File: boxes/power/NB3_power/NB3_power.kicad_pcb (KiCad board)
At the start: 2 copper layers, 80 x 97 mm, 87 parts, among them J1 Barrel_Jack_PJ-036AH-SMT-TR, J2 Conn_01x02_Male, J3 Conn_01x02_Male, J4 Conn_01x02_Male, J5 Conn_01x04_Male, J6 Conn_01x02_Male, J7 Conn_01x02_Male, Q1 PMOS, Q2 NMOS, SW1 SW_SPDT, U1 NiMH_Charger_LTC4010, U2 Voltage_Regulator_AP64501

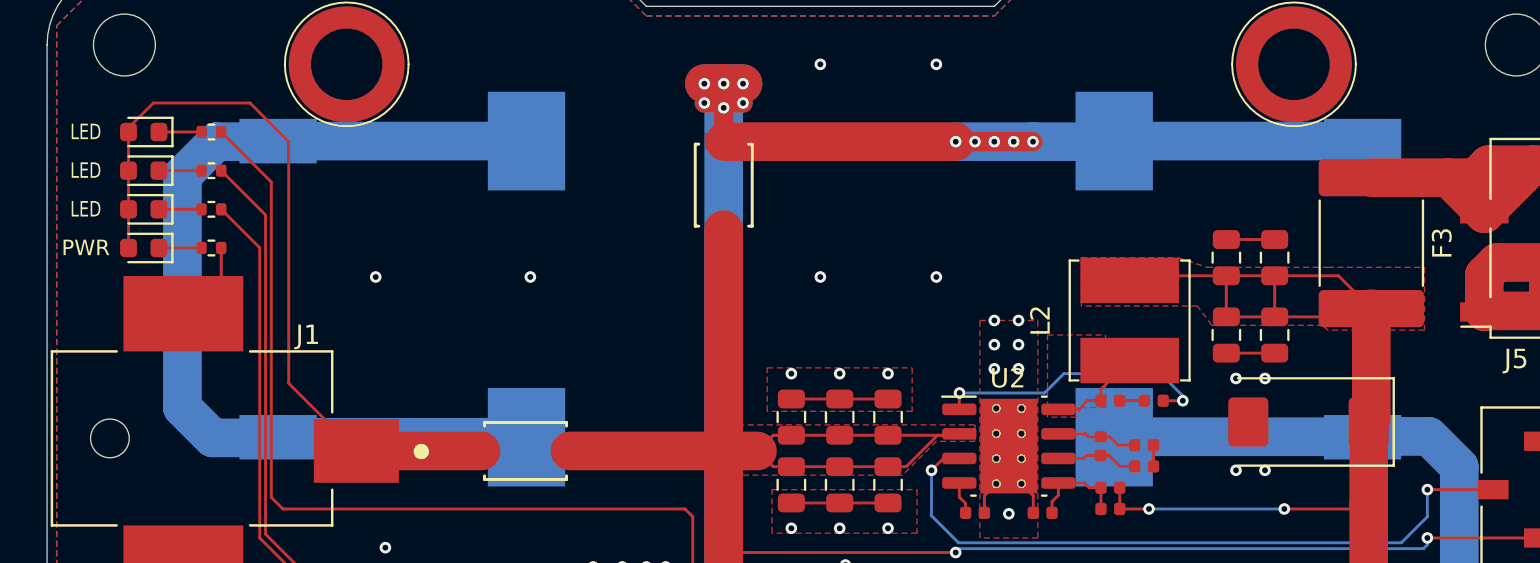
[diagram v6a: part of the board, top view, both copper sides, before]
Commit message: NB3_power PCB fab submisson
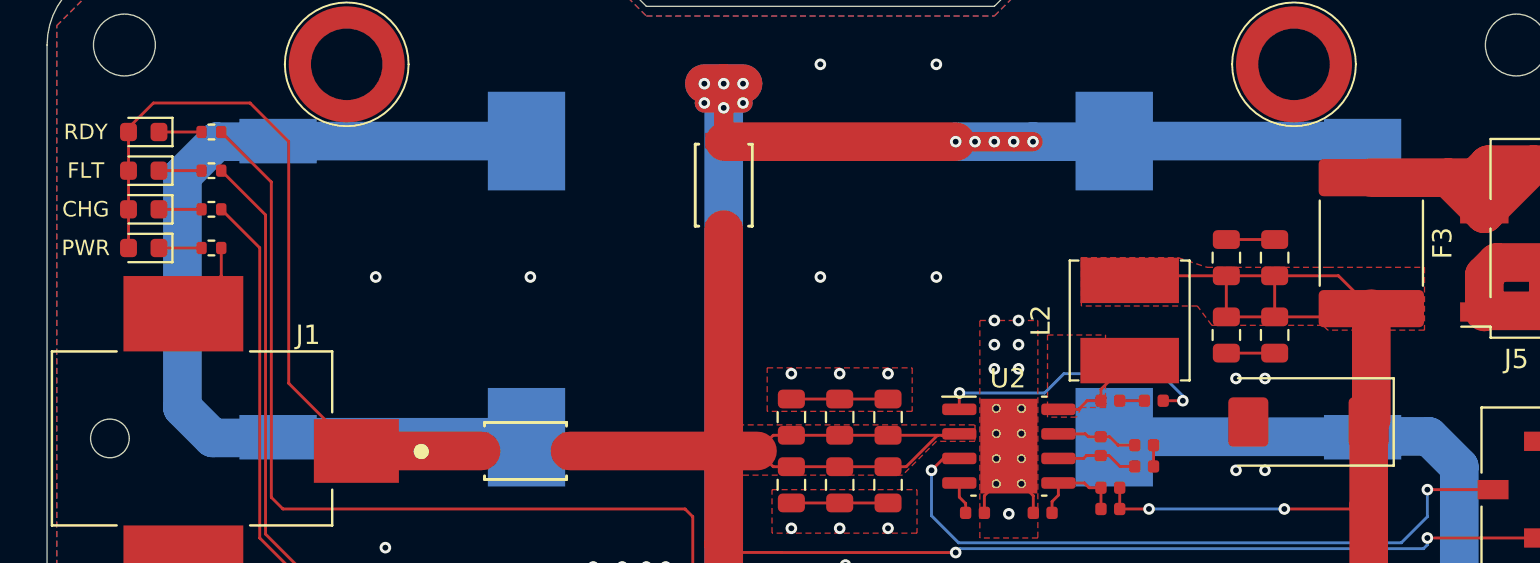
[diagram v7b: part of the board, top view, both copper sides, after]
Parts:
- C1, C2: value 20uF -> 22uF
- R1, R2, R3, R4: value 560 -> 5.6k
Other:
- board text added: "CHG"
- board text added: "FLT"
- board text added: "RDY"
- board text removed: "LED"
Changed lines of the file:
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@@
       (layerselection 0x00010fc_ffffffff)
       (disableapertmacros false)
-      (usegerberextensions false)
+      (usegerberextensions true)
       (usegerberattributes false)
       (usegerberadvancedattributes false)
@@
       (viasonmask false)
       (mode 1)
-      (useauxorigin false)
+      (useauxorigin true)
       (hpglpennumber 1)
       (hpglpenspeed 20)
@@
       (plotreference true)
       (plotvalue true)
-      (plotinvisibletext false)
+      (plotinvisibletext true)
       (sketchpadsonfab false)
       (subtractmaskfromsilk false)
       (outputformat 1)
       (mirror false)
-      (drillshape 1)
+      (drillshape 0)
       (scaleselection 1)
-      (outputdirectory "")
+      (outputdirectory "fab/")
     )
   )
@@
       (effects (font (size 1 1) (thickness 0.15)))
     )
-    (fp_text value "20uF" (at 0 1.65 90) (layer "F.Fab")
+    (fp_text value "22uF" (at 0 1.65 90) (layer "F.Fab")
       (effects (font (size 1 1) (thickness 0.15)))
     )
@@
     (fp_line (start -2.65 -2.15) (end -3.65 -1.15) (layer "F.Fab") (width 0.1))
     (fp_line (start -3.65 -1.15) (end -3.65 2.15) (layer "F.Fab") (width 0.1))
-    (pad "1" smd roundrect (at -3.1125 0 180) (size 2.075 2.55) (layers "F.Cu" "F.Paste" "F.Mask") (roundrect_rratio 0.120482)
+    (pad "1" smd roundrect (at -3.1125 0 180) (size 2.075 2.55) (layers "F.Cu" "F.Paste" "F.Mask") (roundrect_rratio 0.1204819277108434)
       (net 20 "+5V"))
-    (pad "2" smd roundrect (at 3.1125 0 180) (size 2.075 2.55) (layers "F.Cu" "F.Paste" "F.Mask") (roundrect_rratio 0.120482)
+    (pad "2" smd roundrect (at 3.1125 0 180) (size 2.075 2.55) (layers "F.Cu" "F.Paste" "F.Mask") (roundrect_rratio 0.1204819277108434)
       (net 2 "GND"))
     (model "${KISYS3DMOD}/Capacitor_Tantalum_SMD.3dshapes/CP_EIA-7343-31_Kemet-D.wrl"
@@
       (effects (font (size 1 1) (thickness 0.15)))
     )
-    (fp_text value "Conn_01x02_Male" (at 0 3.6 180) (layer "F.Fab")
+    (fp_text value "Conn_01x02_Male" (at 0 3.6 180) (layer "F.Fab") hide
       (effects (font (size 1 1) (thickness 0.15)))
     )
@@
       (effects (font (size 1 1) (thickness 0.15)))
     )
-    (fp_text value "560" (at 0 1.17 180) (layer "F.Fab")
+    (fp_text value "5.6k" (at 0 1.17 180) (layer "F.Fab")
       (effects (font (size 1 1) (thickness 0.15)))
     )
@@
       (effects (font (size 1 1) (thickness 0.15)))
     )
-    (fp_text value "MountingHole_3.2mm_M3" (at 0 4.2) (layer "F.Fab")
+    (fp_text value "MountingHole_3.2mm_M3" (at 0 4.2) (layer "F.Fab") hide
       (effects (font (size 1 1) (thickness 0.15)))
     )
@@
       (effects (font (size 1 1) (thickness 0.15)))
     )
-    (fp_text value "Conn_01x02_Male" (at 0 3.6 -90) (layer "F.Fab")
+    (fp_text value "Conn_01x02_Male" (at 0 3.6 -90) (layer "F.Fab") hide
       (effects (font (size 1 1) (thickness 0.15)))
     )
@@
       (effects (font (size 1 1) (thickness 0.15)))
     )
-    (fp_text value "560" (at 0 1.17) (layer "F.Fab")
+    (fp_text value "5.6k" (at 0 1.17) (layer "F.Fab")
       (effects (font (size 1 1) (thickness 0.15)))
     )
@@
       (effects (font (size 1 1) (thickness 0.15)))
     )
-    (fp_text value "560" (at 0 1.17) (layer "F.Fab")
+    (fp_text value "5.6k" (at 0 1.17) (layer "F.Fab")
       (effects (font (size 1 1) (thickness 0.15)))
     )
@@
     (fp_line (start 3.6775 2.56) (end -3.6775 2.56) (layer "F.Fab") (width 0.1))
     (fp_line (start 3.6775 -2.56) (end 3.6775 2.56) (layer "F.Fab") (width 0.1))
-    (pad "1" smd roundrect (at -3.3875 0 270) (size 1.925 5.45) (layers "F.Cu" "F.Paste" "F.Mask") (roundrect_rratio 0.12987)
+    (pad "1" smd roundrect (at -3.3875 0 270) (size 1.925 5.45) (layers "F.Cu" "F.Paste" "F.Mask") (roundrect_rratio 0.1298701298701299)
       (net 10 "Net-(F3-Pad1)"))
-    (pad "2" smd roundrect (at 3.3875 0 270) (size 1.925 5.45) (layers "F.Cu" "F.Paste" "F.Mask") (roundrect_rratio 0.12987)
+    (pad "2" smd roundrect (at 3.3875 0 270) (size 1.925 5.45) (layers "F.Cu" "F.Paste" "F.Mask") (roundrect_rratio 0.1298701298701299)
       (net 20 "+5V"))
     (model "${KIPRJMOD}/libraries/parts/Fuse_3A_MF-LSMF300X-2/Fuse_3A_MF-LSMF300X-2.stp"
@@
       (effects (font (size 1 1) (thickness 0.15)))
     )
-    (fp_text value "MountingHole_3.2mm_M3" (at 0 4.2) (layer "F.Fab")
+    (fp_text value "MountingHole_3.2mm_M3" (at 0 4.2) (layer "F.Fab") hide
       (effects (font (size 1 1) (thickness 0.15)))
     )
@@
       (effects (font (size 1 1) (thickness 0.15)))
     )
-    (fp_text value "Conn_01x02_Male" (at 0 3.6 -90) (layer "F.Fab")
+    (fp_text value "Conn_01x02_Male" (at 0 3.6 -90) (layer "F.Fab") hide
       (effects (font (size 1 1) (thickness 0.15)))
     )
@@
       (effects (font (size 1 1) (thickness 0.15)))
     )
-    (fp_text value "Conn_01x04_Male" (at 0 6.14 180) (layer "F.Fab")
+    (fp_text value "Conn_01x04_Male" (at 0 6.14 180) (layer "F.Fab") hide
       (effects (font (size 1 1) (thickness 0.15)))
     )
@@
       (effects (font (size 1 1) (thickness 0.15)))
     )
-    (fp_text value "Conn_01x02_Male" (at 0 3.6 180) (layer "F.Fab")
+    (fp_text value "Conn_01x02_Male" (at 0 3.6 180) (layer "F.Fab") hide
       (effects (font (size 1 1) (thickness 0.15)))
     )
@@
       (effects (font (size 1 1) (thickness 0.15)))
     )
-    (fp_text value "Conn_01x02_Male" (at 0 3.6 -90) (layer "F.Fab")
+    (fp_text value "Conn_01x02_Male" (at 0 3.6 -90) (layer "F.Fab") hide
       (effects (font (size 1 1) (thickness 0.15)))
     )
@@
       (effects (font (size 1 1) (thickness 0.15)))
     )
-    (fp_text value "560" (at 0 1.17 180) (layer "F.Fab")
+    (fp_text value "5.6k" (at 0 1.17 180) (layer "F.Fab")
       (effects (font (size 1 1) (thickness 0.15)))
     )
@@
       (effects (font (size 1 1) (thickness 0.15)))
     )
-    (fp_text value "MountingHole_3.2mm_M3" (at 0 4.2) (layer "F.Fab")
+    (fp_text value "MountingHole_3.2mm_M3" (at 0 4.2) (layer "F.Fab") hide
       (effects (font (size 1 1) (thickness 0.15)))
     )
@@
       (effects (font (size 1 1) (thickness 0.15)))
     )
-    (fp_text value "MountingHole_3.2mm_M3" (at 0 4.2) (layer "F.Fab")
+    (fp_text value "MountingHole_3.2mm_M3" (at 0 4.2) (layer "F.Fab") hide
       (effects (font (size 1 1) (thickness 0.15)))
     )
@@
       (effects (font (size 1 1) (thickness 0.15)))
     )
-    (fp_text value "20uF" (at 0 1.65) (layer "F.Fab")
+    (fp_text value "22uF" (at 0 1.65) (layer "F.Fab")
       (effects (font (size 1 1) (thickness 0.15)))
     )
@@
   (gr_line (start 157.05 50.83) (end 159.05 48.83) (layer "Edge.Cuts") (width 0.05))
   (gr_arc (start 186.05 143.83) (end 188.05 143.83) (angle 90) (layer "Edge.Cuts") (width 0.05))
-  (gr_text "LED" (at 110.05 57.33) (layer "F.SilkS")
-    (effects (font (size 0.8 0.6) (thickness 0.15)))
+  (gr_text "RDY" (at 110.05 57.33) (layer "F.SilkS")
+    (effects (font (size 0.8 0.8) (thickness 0.15)))
   )
   (gr_text "NB3 POWER" (at 148.05 129.83) (layer "F.SilkS")
     (effects (font (size 2 2) (thickness 0.3)))
   )
-  (gr_text "LED" (at 110.05 61.33) (layer "F.SilkS")
-    (effects (font (size 0.8 0.6) (thickness 0.15)))
+  (gr_text "CHG" (at 110.05 61.33) (layer "F.SilkS")
+    (effects (font (size 0.8 0.8) (thickness 0.15)))
   )
   (gr_text "PWR" (at 110.05 63.33) (layer "F.SilkS")
     (effects (font (size 0.8 0.8) (thickness 0.15)))
   )
-  (gr_text "LED" (at 110.05 59.33) (layer "F.SilkS")
-    (effects (font (size 0.8 0.6) (thickness 0.15)))
+  (gr_text "FLT" (at 110.05 59.33) (layer "F.SilkS")
+    (effects (font (size 0.8 0.8) (thickness 0.15)))
   )
   (target plus (at 148.05 151.83) (size 5) (width 0.05) (layer "Edge.Cuts"))

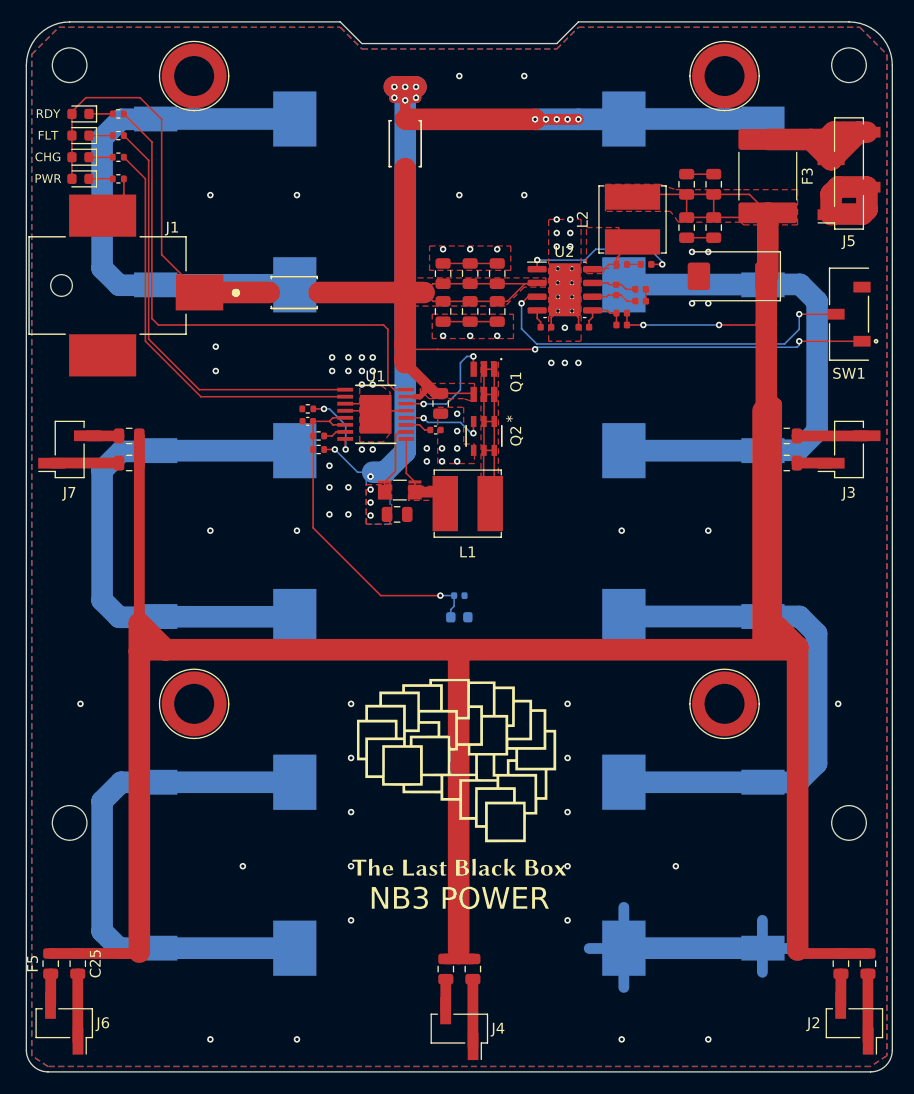
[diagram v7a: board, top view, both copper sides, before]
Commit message: Added new NB3 board drafts (body and power)
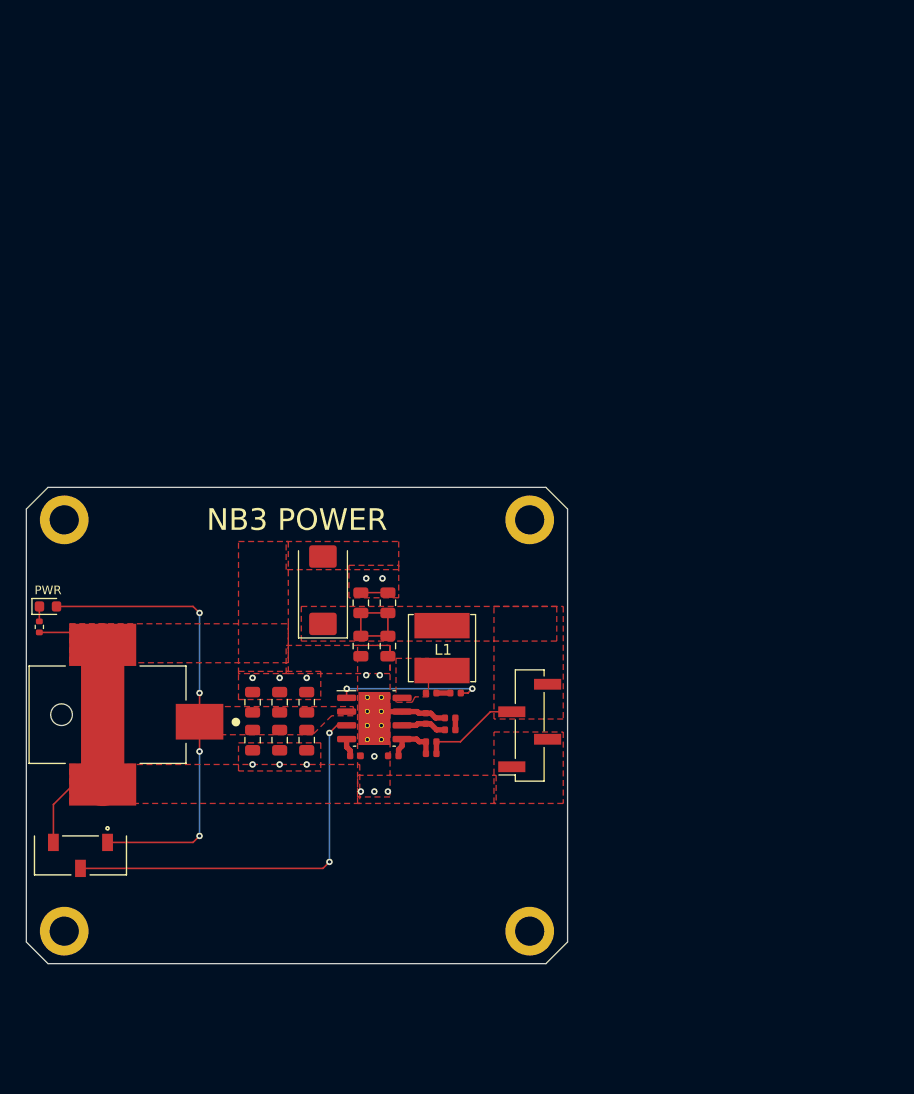
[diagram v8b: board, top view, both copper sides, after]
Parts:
- removed the C1 at (146.3, 84.1)
- removed the C2 at (142.3, 94.3)
- removed C22, C23, C24, C25, C26: 10uF, Capacitor_SMD:C_0805_2012Metric
- removed the C3 at (145.8, 86.5)
- removed the C4 at (134.1, 85.7)
- removed the C5 at (148.1, 101.8)
- removed CR1, CR2: Schottky_PMEG3050EP,115, NB3_power:Schottky_PMEG3050EP,115
- removed the D1 at (113.0, 57.3)
- removed D2, D3: LED, LED_SMD:LED_0603_1608Metric
- removed F1, F2, F4, F5, F6: 1.1h2.2t, Fuse:Fuse_0805_2012Metric
- removed F3: 3h5t, Fuse:Fuse_2920_7451Metric
- removed G***: LOGO, NB3_power:Logo_LBB_25mm
- removed G***: LOGO, NB3_power:Logo_VK_15mm
- removed the J2 at (184.6, 141.3)
- removed J3, J4, J6, J7: Conn_01x02_Male, Connector_PinHeader_2.54mm:PinHeader_1x02_P2.54mm_Vertical_SMD_Pin1Right
- removed the L1 at (148.8, 93.3)
- removed Q1: PMOS, NB3_power:PMOS_SMD_FDC658AP
- removed Q2: NMOS, NB3_power:NMOS_SMD_SI3410DV-T1-GE3
- removed the R1 at (116.5, 57.3)
- removed the R2 at (116.5, 59.3)
- removed the R3 at (116.5, 61.3)
- removed the R5 at (142.6, 92.1)
- removed R6: 49.9k, Resistor_SMD:R_0402_1005Metric
- removed R7: 50k, Resistor_SMD:R_0402_1005Metric
- removed R8: 10k, Resistor_SMD:R_0402_1005Metric
- removed REF** (x4): MountingHole_3.2mm_M3, MountingHole:MountingHole_3.2mm_M3
- removed TH1: 10k, 3750, Resistor_SMD:R_0603_1608Metric
- removed the U1 at (140.3, 85.1)
- removed XB1, XB10, XB11, XB12, XB2, XB3, XB4, XB5, XB6, XB7, XB8, XB9: SMD_AA_Clip_Keystone_53TR, NB3_power:SMD_AA_Clip_Keystone_53TR
- H1, H2, H3, H4: value Standoff_SMT_5H_M2.5_9774050151R -> MountingHole; footprint NB3_power:Standoff_SMT_5H_M2.5_9774050151R -> MountingHole:MountingHole_2.7mm_M2.5_ISO7380_Pad
- moved SW1 86.8 mm to (113.0, 125.8), turned to 180 degrees
- moved J2 58.9 mm to (154.6, 113.8)
- moved C13 53.7 mm to (138.9, 106.5), turned to -90 degrees
- moved C12 50.8 mm to (141.4, 106.5), turned to -90 degrees
- moved C16 47.7 mm to (135.4, 101.3), turned to 90 degrees
- moved C14 47.6 mm to (138.9, 102.5), turned to 90 degrees
- moved H2 44.8 mm to (154.6, 94.8)
- moved C15 44.3 mm to (141.4, 102.5), turned to 90 degrees
- moved C1 43.3 mm to (131.4, 115.2)
- moved C11 43.3 mm to (145.4, 116.4)
- moved C2 43.3 mm to (133.9, 115.2)
- moved C3 43.3 mm to (128.9, 115.2)
- moved C4 43.3 mm to (128.9, 111.7)
- moved C5 43.3 mm to (131.4, 111.7)
- moved C6 43.3 mm to (133.9, 111.7)
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- renumbered C13 to C1, C21 to C10, C12 to C11, C6 to C12, C7 to C13, C8 to C14, C9 to C15, C10 to C16, C14 to C2, C15 to C3, C16 to C4, C17 to C5, C18 to C6, C11 to C7, C19 to C8, C20 to C9, D4 to D1, J5 to J2, L2 to L1, R4 to R1, R9 to R2, R11 to R3, R10 to R4, R12 to R5, U2 to U1
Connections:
- C1 pad 1: /VIN -> +12V
- C2 pad 1: /VIN -> +12V
- C3 pad 1: /VIN -> +12V
- C4 pad 1: /VIN -> +12V
- C5 pad 1: /VIN -> +12V
- C6 pad 1: /VIN -> +12V
- H1 pad 1: Net-(H1-Pad1) -> (no net)
- H2 pad 1: Net-(H2-Pad1) -> (no net)
- H3 pad 1: Net-(H3-Pad1) -> (no net)
- H4 pad 1: Net-(H4-Pad1) -> (no net)
- J2 pad 3: Net-(F3-Pad1) -> +5V
- J2 pad 4: Net-(F3-Pad1) -> +5V
- SW1 pad 1: /VIN -> +12V
- U1 pad 2: /VIN -> +12V
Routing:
- net +5V: track 292.4 -> 19.0 mm, vias 2 -> 0
- net /VIN: track 103.4 -> 0.00 mm, vias 2 -> 0
- net /VBAT: track 97.2 -> 0.00 mm, vias 16 -> 0
- net GND: track 108.8 -> 37.7 mm, vias 75 -> 14
- net Net-(R1-Pad2): track 49.1 -> 0.00 mm
- net Net-(XB7-Pad1): track 49.0 -> 0.00 mm
- net Net-(XB6-Pad1): track 49.0 -> 0.00 mm
- net Net-(XB3-Pad1): track 49.0 -> 0.00 mm
- net Net-(XB2-Pad1): track 49.0 -> 0.00 mm
- net Net-(XB10-Pad1): track 49.0 -> 0.00 mm
- net Net-(R2-Pad2): track 39.8 -> 0.00 mm
- net Net-(R3-Pad2): track 38.4 -> 0.00 mm
- net Net-(C4-Pad1): track 32.3 -> 0.00 mm, vias 1 -> 0
- net /Drain: track 29.0 -> 0.00 mm
- net Net-(F3-Pad1): track 20.4 -> 0.00 mm
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- added copper zone on F.Cu, net +12V
- removed copper zone on F.Cu, net /Drain
- removed copper zone on B.Cu, net /VBAT
- removed copper zone on F.Cu, net /VBAT
- removed copper zone on F.Cu, net /VIN
- removed copper zone on B.Cu, net GND
- removed copper zone on F.Cu, net Net-(L1-Pad2)
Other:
- board size 80 x 97 mm -> 50 x 44 mm
- board text removed: "CHG"
- board text removed: "FLT"
- board text removed: "RDY"
